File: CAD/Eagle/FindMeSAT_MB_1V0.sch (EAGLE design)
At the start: 131 parts, among them J291 MCX-J-P-X-RA-SM1, J685 SMA_CON, J701 MOLEX_105017-0001, J801 MICROSIM-8P_SDCARD-8P_MOLEX-1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, J901 JST_S3B-XH-A, Q101 ABS07-32.768KHZ, Q651 ABM3B-16MHZ-10-R50-1-U, U1001 CFPT-141-20MHZ, U101 ATXMEGA256A3BU-AU, U1011 OPA354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

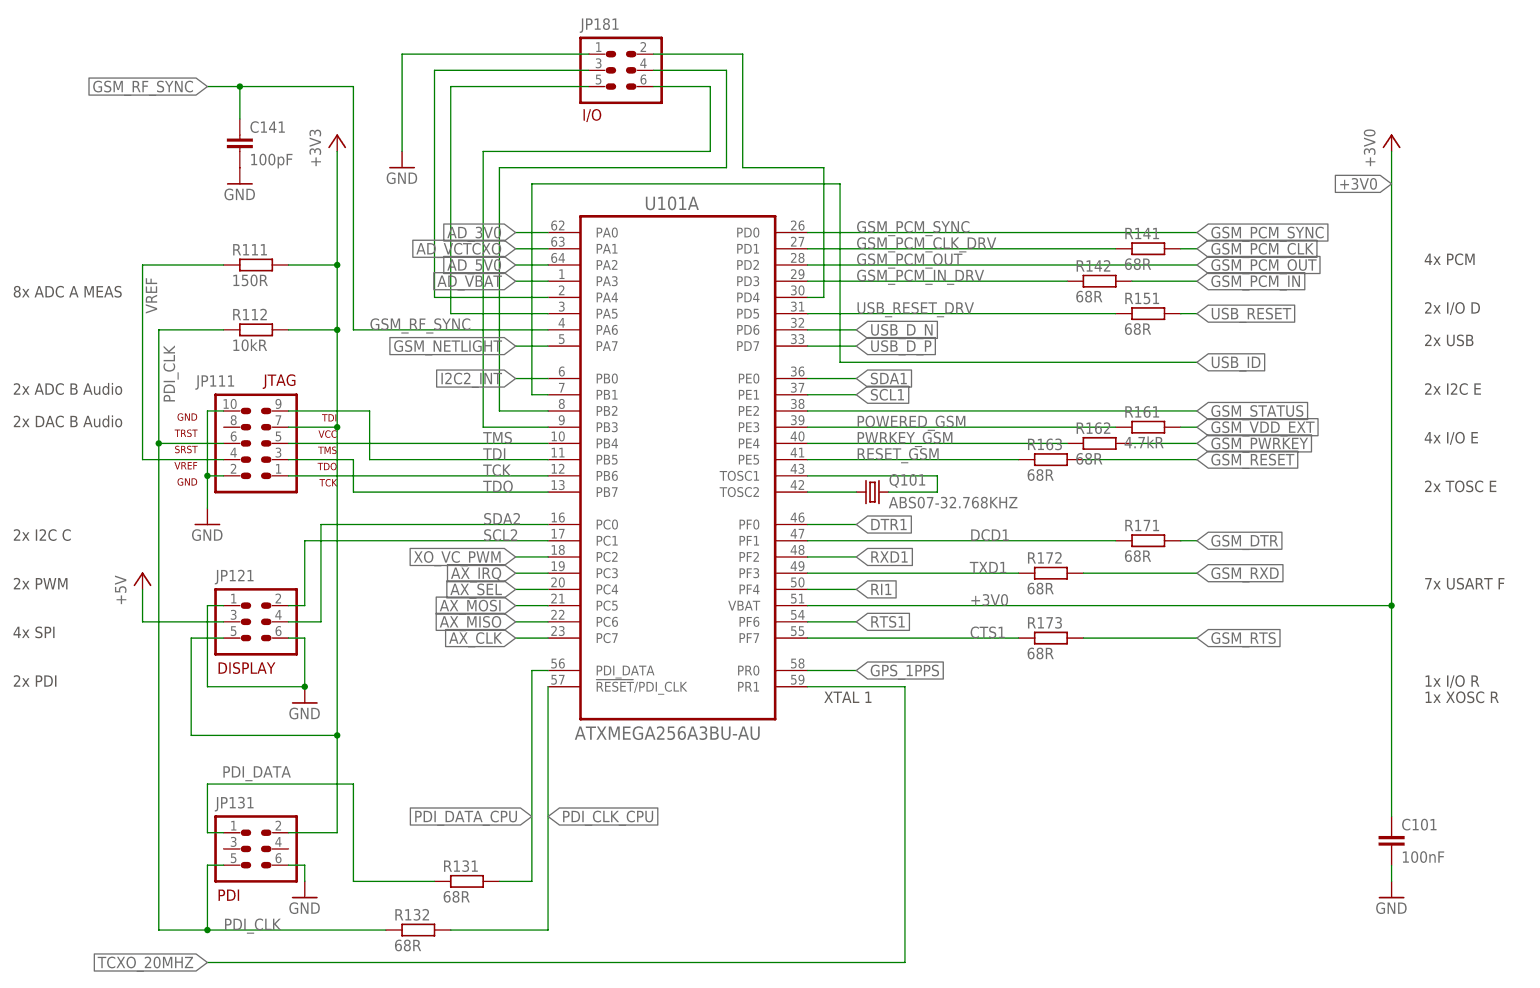
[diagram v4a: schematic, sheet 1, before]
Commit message: Eagle - replaced 10uH device by a 0603 package, optional Gfx-LCD added to the Docs
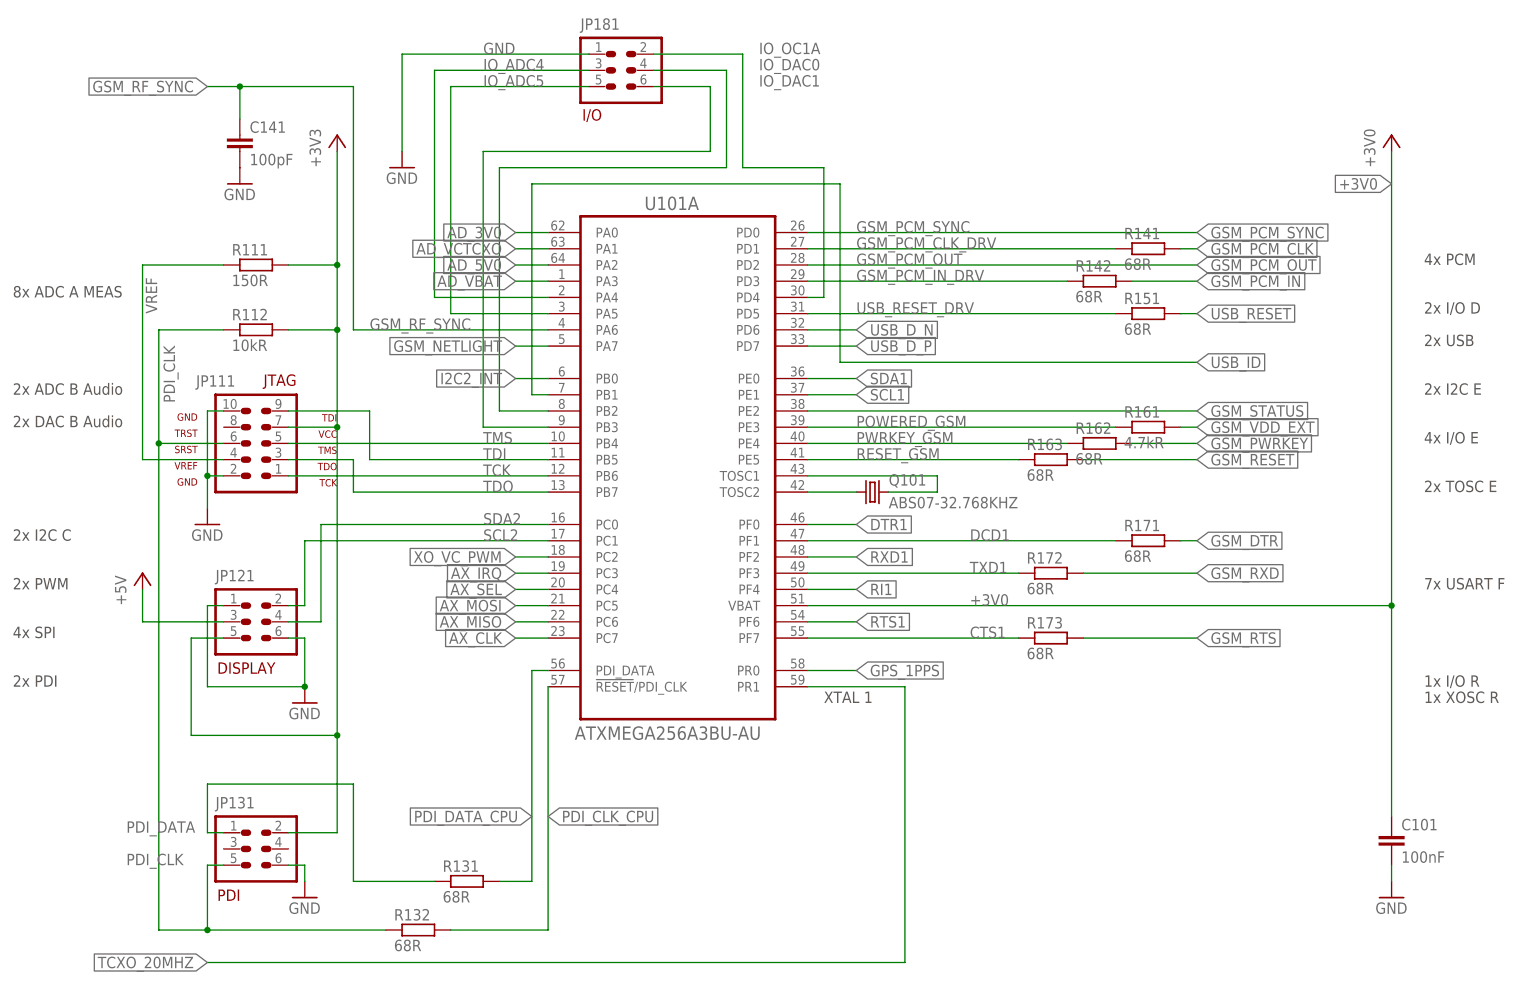
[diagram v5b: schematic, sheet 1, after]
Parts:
- L191: device rcl:L-EUL5650M -> rcl:R-EU_R0603
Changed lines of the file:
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@@
 <part name="GND1092" library="df4iah_supply" deviceset="GND" device=""/>
 <part name="+3V3_1091" library="df4iah_supply" deviceset="+3V3" device=""/>
-<part name="L191" library="rcl" deviceset="L-EU" device="L5650M" value="10uH"/>
+<part name="L191" library="rcl" deviceset="R-EU_" device="R0603" value="10uH"/>
 <part name="C191" library="rcl" deviceset="C-EU" device="C0603" value="100nF"/>
 <part name="C193" library="rcl" deviceset="C-EU" device="C0603" value="100nF"/>
@@
 <pinref part="JP181" gate="G$1" pin="1"/>
 <wire x1="66.04" y1="167.64" x2="95.25" y2="167.64" width="0.1524" layer="91"/>
+<label x="78.74" y="167.64" size="1.778" layer="95"/>
 </segment>
 </net>
@@
 <pinref part="JP131" gate="G$1" pin="1"/>
 <wire x1="35.56" y1="45.72" x2="38.1" y2="45.72" width="0.1524" layer="91"/>
-<label x="37.846" y="54.356" size="1.778" layer="95"/>
+<label x="22.86" y="45.72" size="1.778" layer="95"/>
 </segment>
 </net>
@@
 <junction x="27.94" y="106.68"/>
 <pinref part="JP111" gate="G$1" pin="6"/>
-<label x="38.1" y="30.48" size="1.778" layer="95"/>
+<label x="22.86" y="40.64" size="1.778" layer="95"/>
 <label x="30.48" y="113.03" size="1.778" layer="95" rot="R90"/>
 </segment>
@@
 <pinref part="JP181" gate="G$1" pin="3"/>
 <wire x1="71.12" y1="165.1" x2="95.25" y2="165.1" width="0.1524" layer="91"/>
+<label x="78.74" y="165.1" size="1.778" layer="95"/>
 </segment>
 </net>
@@
 <pinref part="JP181" gate="G$1" pin="5"/>
 <wire x1="73.66" y1="162.56" x2="95.25" y2="162.56" width="0.1524" layer="91"/>
+<label x="78.74" y="162.56" size="1.778" layer="95"/>
 </segment>
 </net>
@@
 <pinref part="U101" gate="A" pin="PD4"/>
 <wire x1="132.08" y1="129.54" x2="129.54" y2="129.54" width="0.1524" layer="91"/>
+<label x="121.92" y="167.64" size="1.778" layer="95"/>
 </segment>
 </net>
@@
 <wire x1="116.84" y1="165.1" x2="105.41" y2="165.1" width="0.1524" layer="91"/>
 <pinref part="JP181" gate="G$1" pin="4"/>
+<label x="121.92" y="165.1" size="1.778" layer="95"/>
 </segment>
 </net>
@@
 <wire x1="114.3" y1="162.56" x2="105.41" y2="162.56" width="0.1524" layer="91"/>
 <pinref part="JP181" gate="G$1" pin="6"/>
+<label x="121.92" y="162.56" size="1.778" layer="95"/>
 </segment>
 </net>
@@
 <instance part="GND1092" gate="1" x="127" y="27.94"/>
 <instance part="+3V3_1091" gate="G$1" x="25.4" y="81.28"/>
-<instance part="L191" gate="G$1" x="33.02" y="50.8" rot="R270"/>
+<instance part="L191" gate="G$1" x="33.02" y="50.8" smashed="yes" rot="R180">
+<attribute name="NAME" x="29.21" y="52.2986" size="1.778" layer="95"/>
+<attribute name="VALUE" x="29.21" y="47.498" size="1.778" layer="96"/>
+</instance>
 <instance part="C191" gate="G$1" x="45.72" y="45.72"/>
 <instance part="C193" gate="G$1" x="55.88" y="45.72"/>

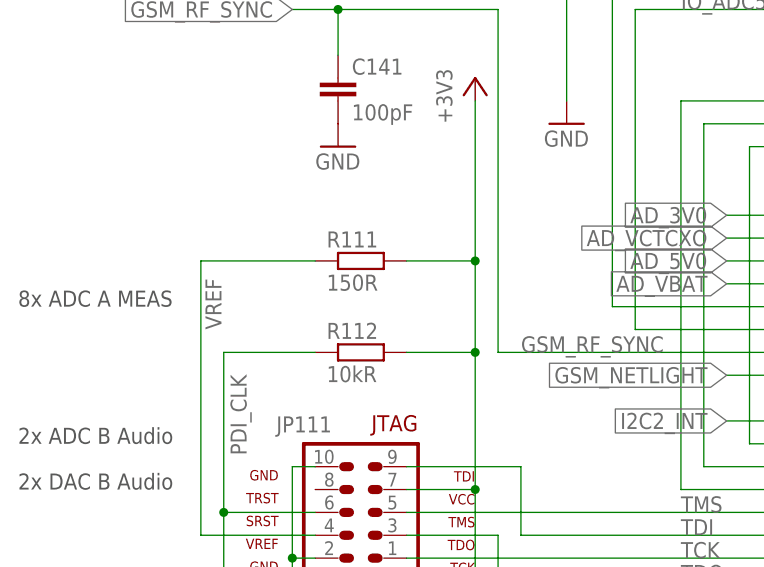
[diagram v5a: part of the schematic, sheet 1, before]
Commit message: CAD - JTAG resistor for Vref changed from 150 ohms to 0 ohms
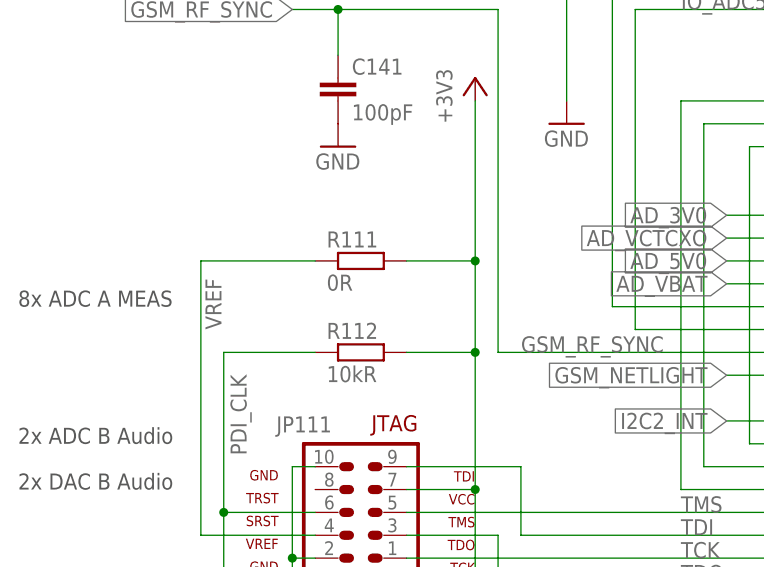
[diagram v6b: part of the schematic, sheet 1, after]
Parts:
- R111: value 150R -> 0R
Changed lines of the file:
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@@
 <part name="JP111" library="df4iah_connector" deviceset="AVR-JTAG-10" device="" value=""/>
 <part name="GND111" library="df4iah_supply" deviceset="GND" device=""/>
-<part name="R111" library="rcl" deviceset="R-EU_" device="R0805" value="150R"/>
+<part name="R111" library="rcl" deviceset="R-EU_" device="R0805" value="0R"/>
 <part name="J901" library="df4iah_connector" deviceset="JST_S3B-XH-A" device=""/>
 <part name="C901" library="rcl" deviceset="C-EU" device="C0805" value="100uF"/>
